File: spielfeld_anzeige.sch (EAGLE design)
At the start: 19 parts, among them IC1 UDN2981A, IC2 UDN2981A, IC3 74HC595N, IC4 74HC595N, IC5 74HC595N

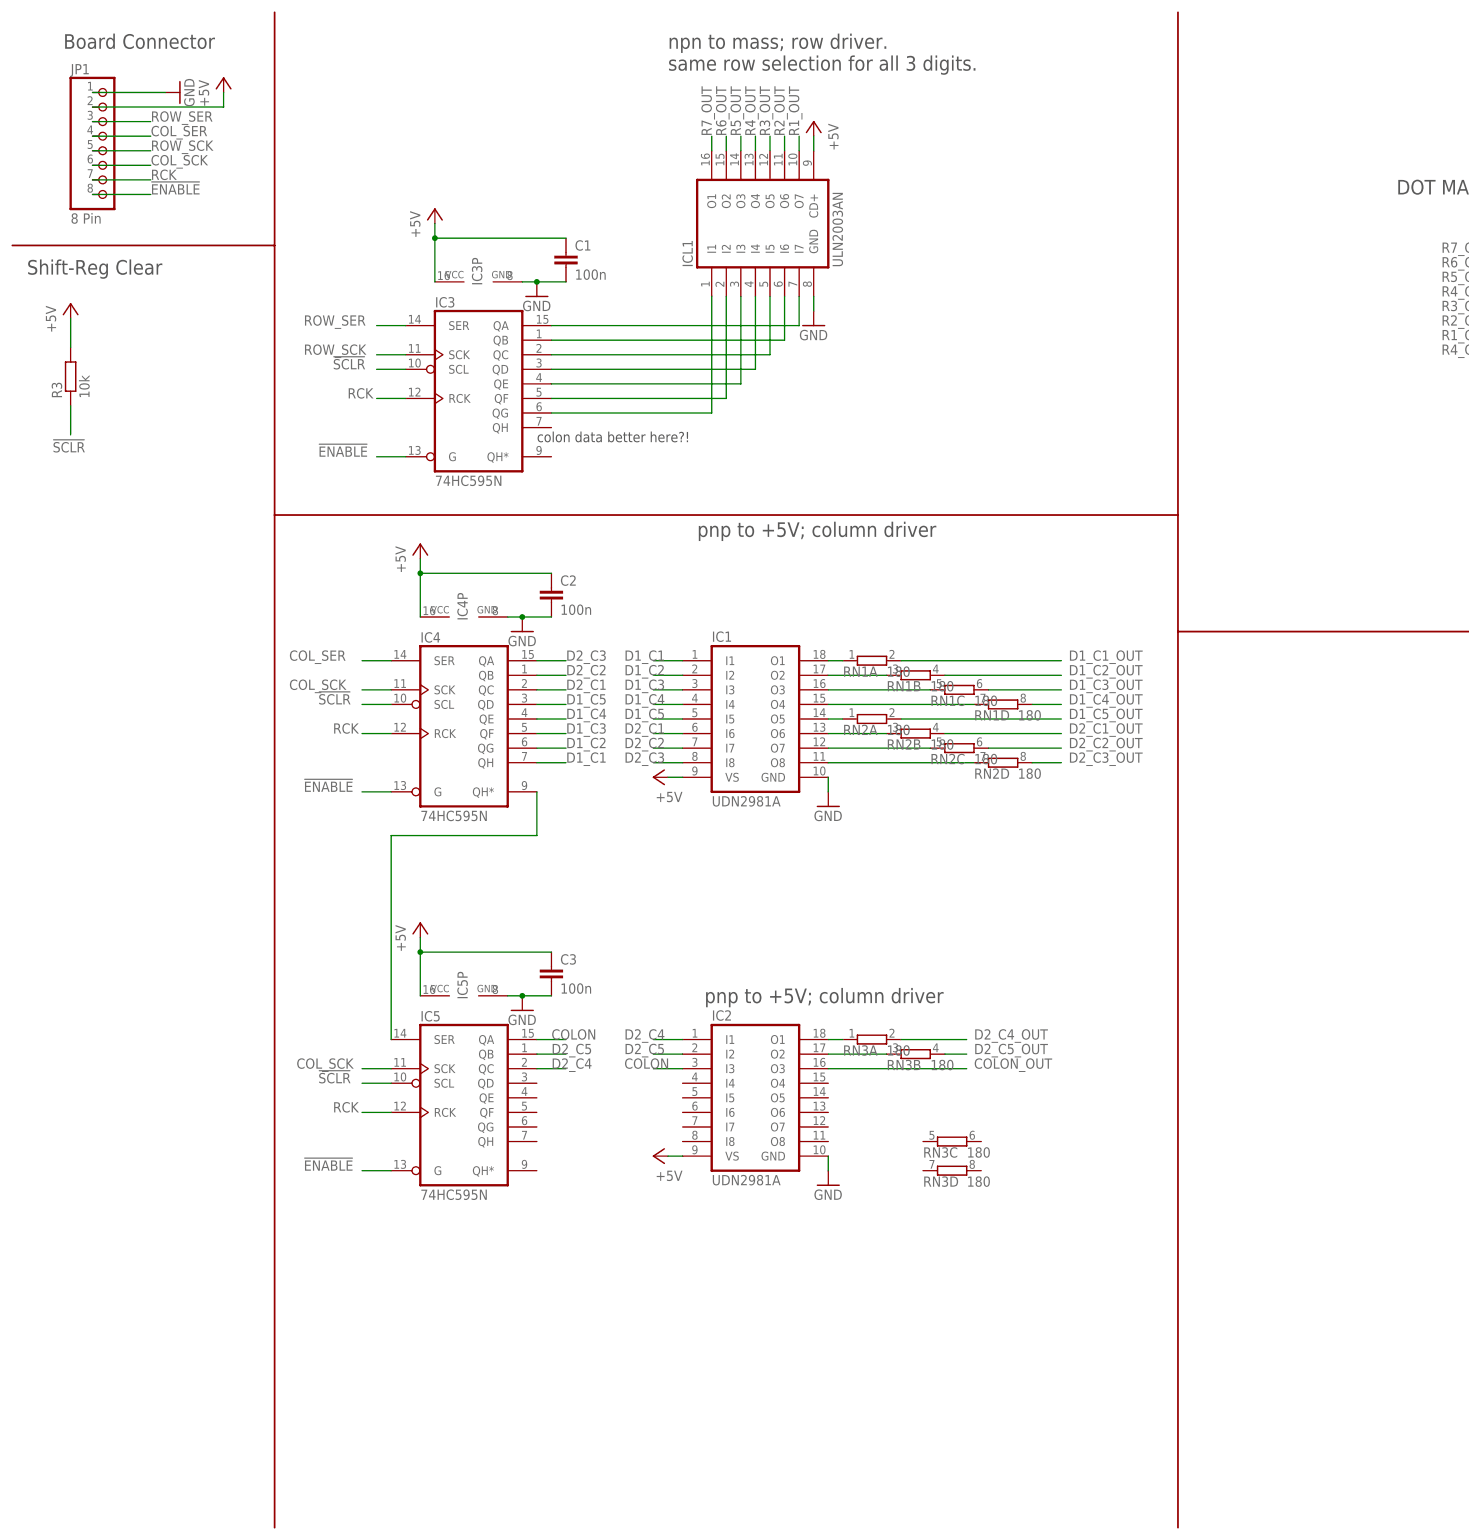
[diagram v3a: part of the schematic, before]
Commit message: Revision due to Pete and Leander on 30.04.2018
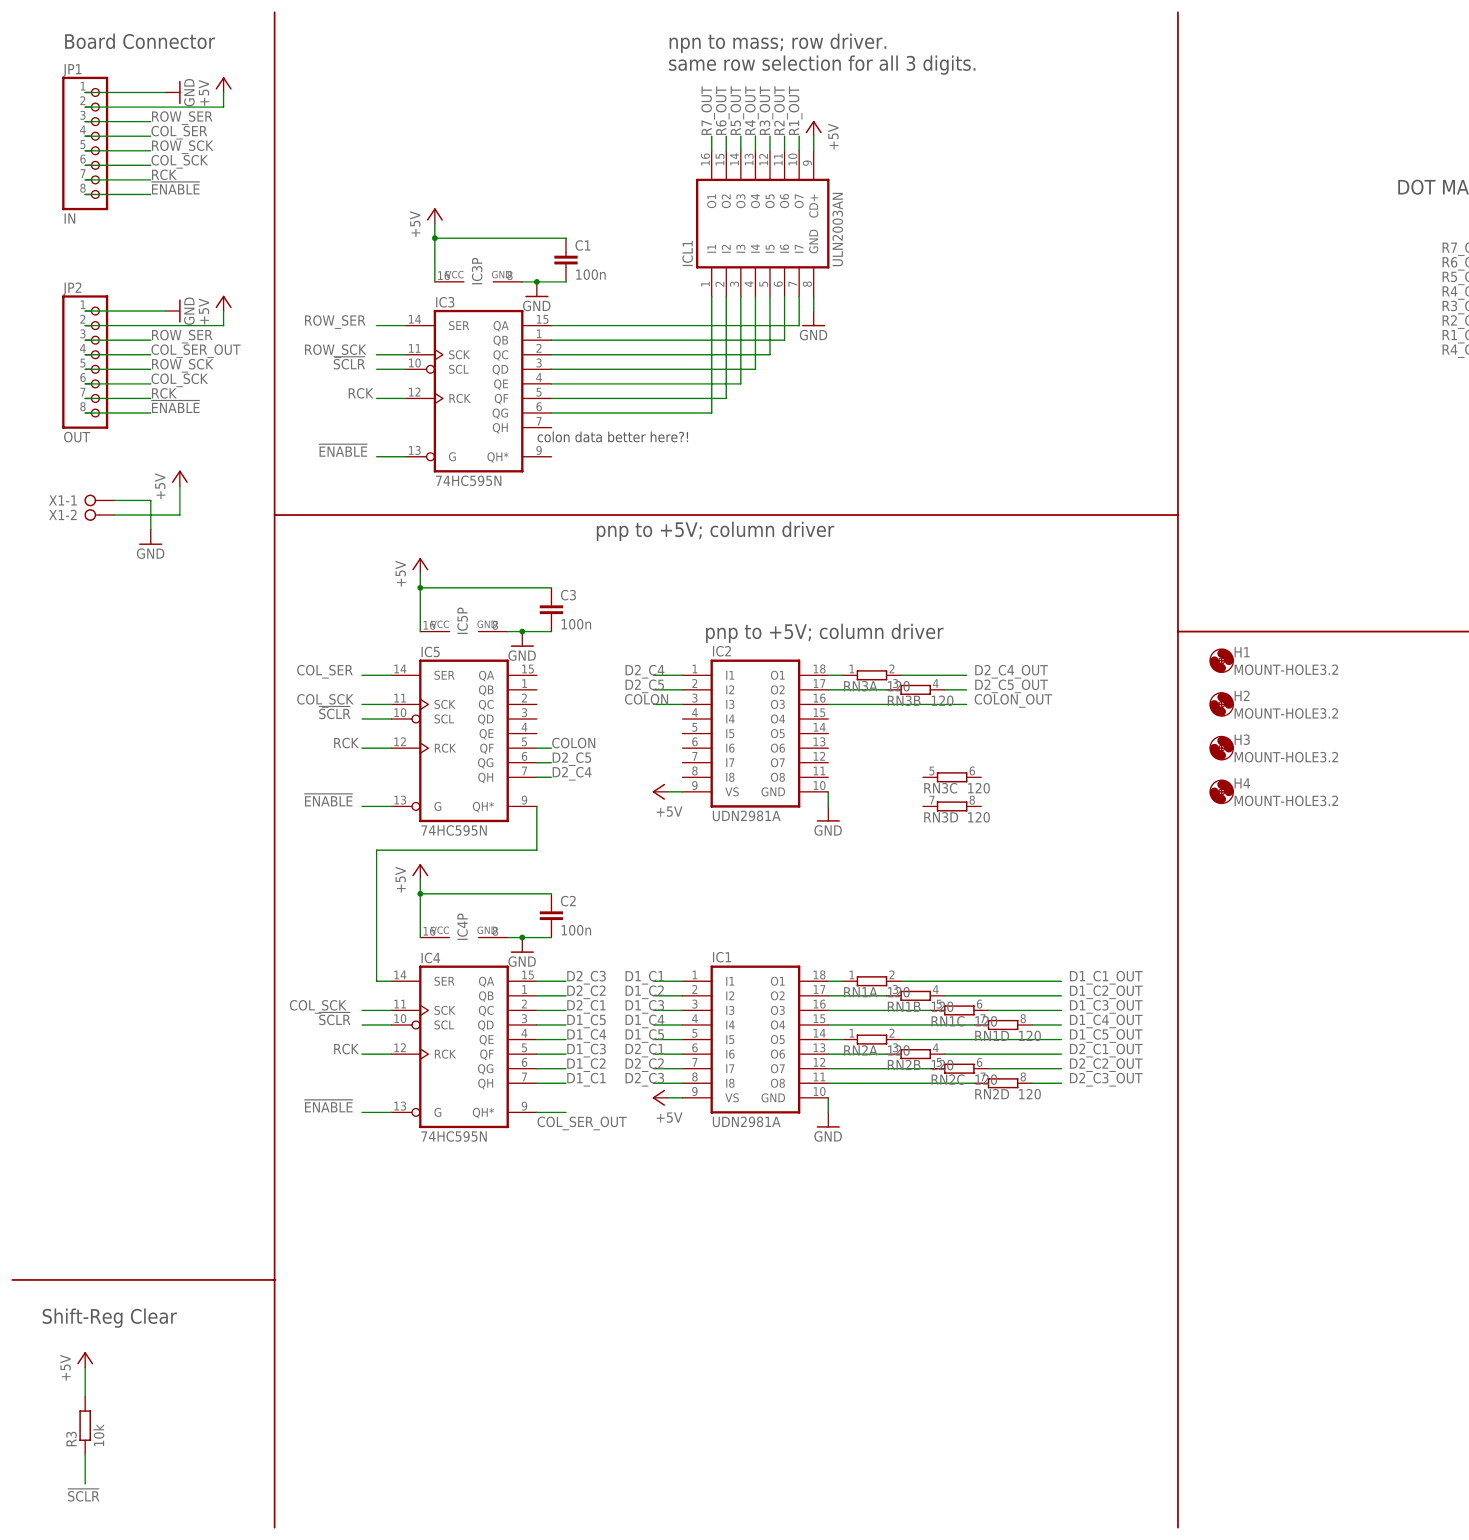
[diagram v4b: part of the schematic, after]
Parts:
- added H1, H2, H3, H4: MOUNT-HOLE3.2, holes:MOUNT-HOLE3.2
- added JP2: OUT, pinhead:PINHD-1X8
- added X1: (no value), con-wago-508:W237-02P
- JP1: value 8 Pin -> IN; device pinhead:PINHD-1X8/90 -> pinhead:PINHD-1X8
- RN1, RN2, RN3: value 180 -> 120
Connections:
- new net COL_SER_OUT: IC4A.QH*, JP2.4
- net !ENABLE!: now also JP2.8
- net +5V: now also JP2.2, X1-2.KL
- net COLON: now also IC5A.QF; no longer IC5A.QA
- net COL_SCK: now also JP2.6
- net COL_SER: now also IC5A.SER; no longer IC4A.SER
- net D2_C4: now also IC5A.QH; no longer IC5A.QC
- net D2_C5: now also IC5A.QG; no longer IC5A.QB
- net GND: now also JP2.1, X1-1.KL
- net N$20: now also IC4A.SER, IC5A.QH*; no longer IC4A.QH*, IC5A.SER
- net RCK: now also JP2.7
- net ROW_SCK: now also JP2.5
- net ROW_SER: now also JP2.3
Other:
- moved on the sheet: C2, C3, IC1, IC2, IC4, IC4P, IC5, IC5P, JP1, R3, RN1A, RN1B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

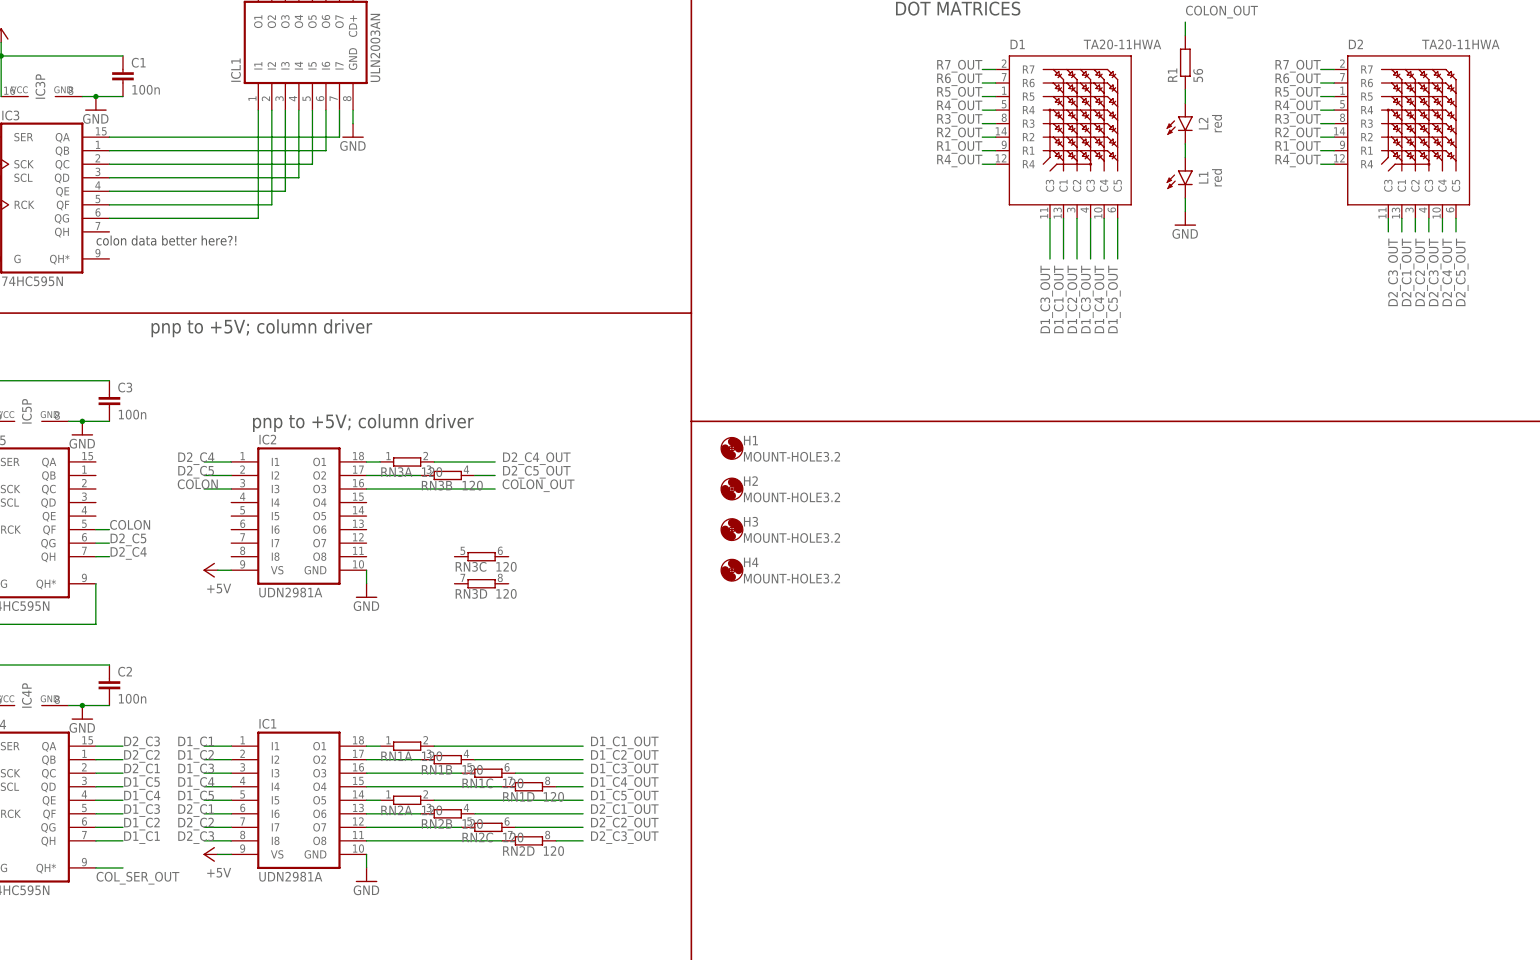
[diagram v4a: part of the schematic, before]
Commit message: Changed Layout (in Progress)
Updated Eagle-Borad and Schematic
- Reorganize the outputs of the FFs
- Move Colon to FF for Rows
- Change resistors to 0805 and 82 Ohm
- Put all devices in Layout back to 50 mil grid
- startet layout from scratch
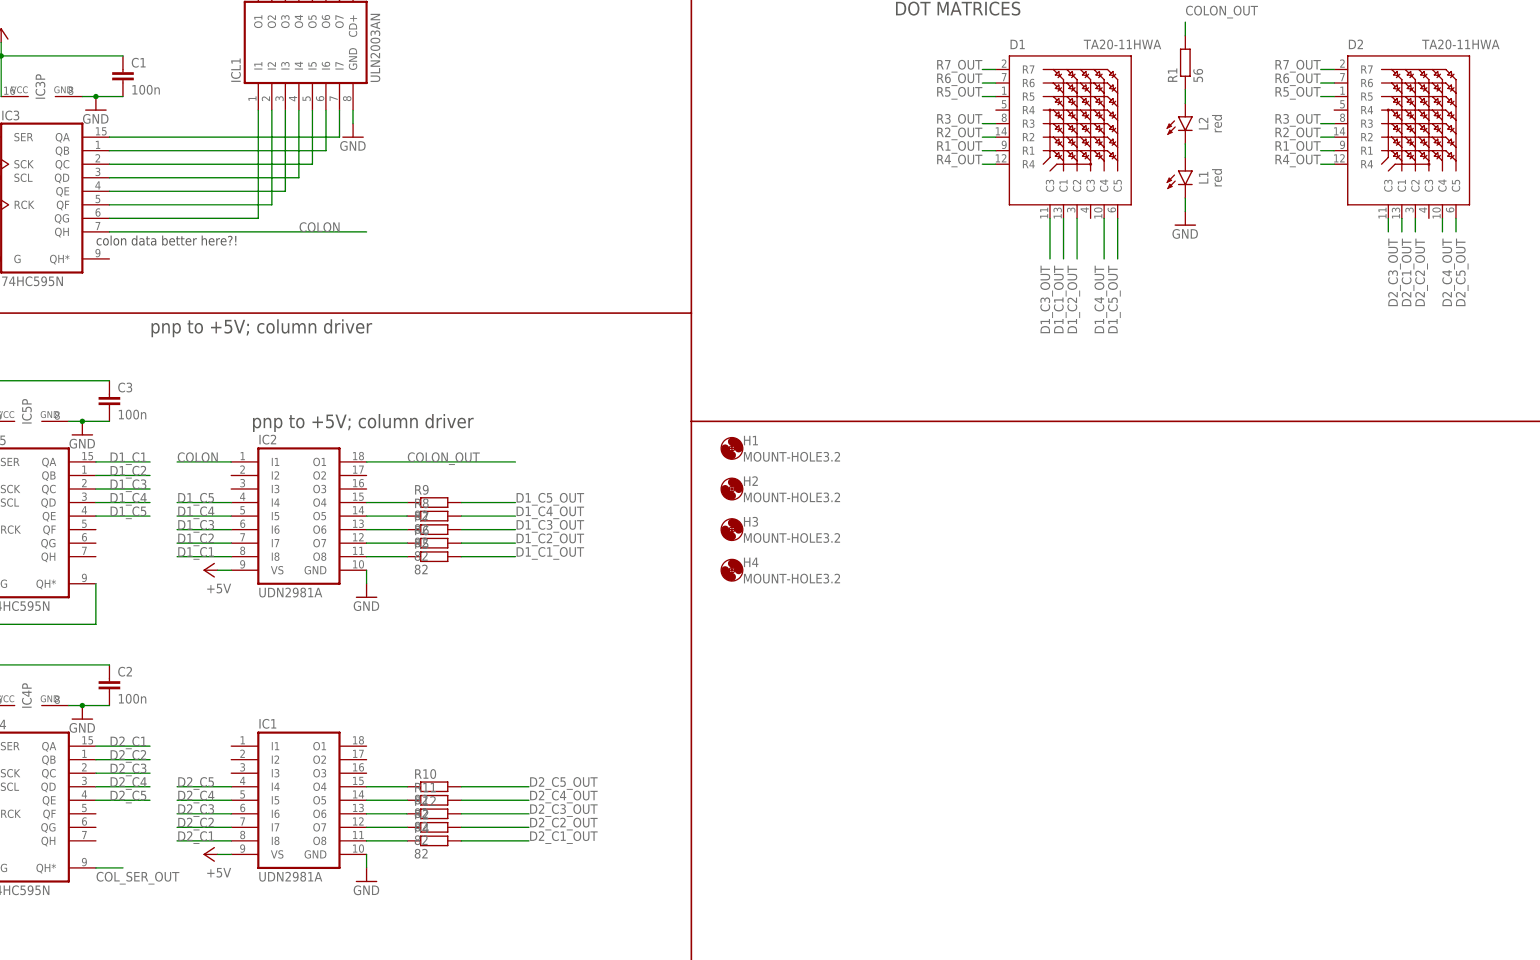
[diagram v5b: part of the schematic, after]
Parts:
- removed RN1, RN2, RN3: 120, resistor-sil:E4R
- added R10, R11, R12, R2, R4, R5, R6, R7, R8, R9: 82, rcl:R-EU_R0805
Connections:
- net COLON: now also IC2.I1, IC3A.QH; no longer IC2.I3, IC5A.QF
- net COLON_OUT: now also IC2.O1; no longer IC2.O3
- net D1_C1: now also IC2.I8, IC5A.QA; no longer IC1.I1, IC4A.QH
- net D1_C1_OUT: now also R5.2; no longer RN1A.2
- net D1_C2: now also IC2.I7, IC5A.QB; no longer IC1.I2, IC4A.QG
- net D1_C2_OUT: now also R6.2; no longer RN1B.2
- net D1_C3: now also IC2.I6, IC5A.QC; no longer IC1.I3, IC4A.QF
- net D1_C3_OUT: now also R7.2; no longer D1.C3, RN1C.2
- net D1_C4: now also IC2.I5, IC5A.QD; no longer IC1.I4, IC4A.QE
- net D1_C4_OUT: now also R8.2; no longer RN1D.2
- net D1_C5: now also IC2.I4, IC5A.QE; no longer IC1.I5, IC4A.QD
- net D1_C5_OUT: now also R9.2; no longer RN2A.2
- net D2_C1: now also IC1.I8, IC4A.QA; no longer IC1.I6, IC4A.QC
- net D2_C1_OUT: now also R4.2; no longer RN2B.2
- net D2_C2_OUT: now also R2.2; no longer RN2C.2
- net D2_C3: now also IC1.I6, IC4A.QC; no longer IC1.I8, IC4A.QA
- net D2_C3_OUT: now also R12.2; no longer D2.C3, RN2D.2
- net D2_C4: now also IC1.I5, IC4A.QD; no longer IC2.I1, IC5A.QH
- net D2_C4_OUT: now also R11.2; no longer RN3A.2
- net D2_C5: now also IC1.I4, IC4A.QE; no longer IC2.I2, IC5A.QG
- net D2_C5_OUT: now also R10.2; no longer RN3B.2
- net N$14: now also R11.1; no longer RN2A.1
- net N$15: now also R12.1; no longer RN2B.1
- net N$16: now also R2.1; no longer RN2C.1
- net N$17: now also R4.1; no longer RN2D.1
- net N$2: now also IC2.O8, R5.1; no longer IC1.O1, RN1A.1
- net N$3: now also IC2.O7, R6.1; no longer IC1.O2, RN1B.1
- net N$4: now also IC2.O6, R7.1; no longer IC1.O3, RN1C.1
- net N$5: now also IC2.O5, R8.1; no longer IC1.O4, RN1D.1
- net N$6: now also IC2.O4, R9.1; no longer IC2.O1, RN3A.1
- net N$7: now also IC1.O4, R10.1; no longer IC2.O2, RN3B.1
- net R4_OUT: no longer D1.R4, D2.R4
